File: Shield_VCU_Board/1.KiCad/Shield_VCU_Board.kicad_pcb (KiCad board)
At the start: 2 copper layers, 250.5 x 107.1 mm, 161 parts, among them J1 Conn_02x08_Odd_Even, J10 Main_Supply, J11 Conn_01x40_Socket, J13 Conn_Molex_TouchPanel, J14 CAN_OUT, J15 Conn_01x04_Socket, J2 Conn_02x10_Odd_Even, J3/1 NXP3, J4 Conn_02x08_Odd_Even, J5 Conn_02x10_Odd_Even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

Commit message: NewSupplyArchitecture - v0.1
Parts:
- removed C22, C23: 10uF, Capacitor_Tantalum_SMD:CP_EIA-2012-12_Kemet-R_HandSolder
- removed C46: 0.1uF, Capacitor_SMD:C_0805_2012Metric_Pad1.18x1.45mm_HandSolder
- removed D5, D6: 1N4002, Diode_SMD:D_SOD-123
- removed R57: 660, Resistor_SMD:R_1206_3216Metric_Pad1.30x1.75mm_HandSolder
- removed R58: 1.1k, Resistor_SMD:R_1206_3216Metric_Pad1.30x1.75mm_HandSolder
- removed U11: LM317_SOT-223, Package_TO_SOT_SMD:SOT-223-3_TabPin2
- added C45: 0.1uF, Capacitor_SMD:C_0805_2012Metric_Pad1.18x1.45mm_HandSolder, B.Cu at (44.6, 144.7)
- added C47: 10uF, Capacitor_SMD:C_1210_3225Metric_Pad1.33x2.70mm_HandSolder, B.Cu at (54.3, 147.6)
- added C48: 22uF, Capacitor_SMD:C_0805_2012Metric_Pad1.18x1.45mm_HandSolder, B.Cu at (54.1, 142.0)
- added C49: 0.1uF, Capacitor_SMD:C_0805_2012Metric_Pad1.18x1.45mm_HandSolder, B.Cu at (103.6, 134.5)
- added C50: 0.1uF, Capacitor_SMD:C_0805_2012Metric_Pad1.18x1.45mm_HandSolder, B.Cu at (99.4, 141.2)
- added C51: 22uF, Capacitor_SMD:C_0805_2012Metric_Pad1.18x1.45mm_HandSolder, B.Cu at (98.2, 132.9)
- added C52: 22uF, Capacitor_SMD:C_0805_2012Metric_Pad1.18x1.45mm_HandSolder, B.Cu at (52.1, 141.9)
- added C53: 22uF, Capacitor_SMD:C_0805_2012Metric_Pad1.18x1.45mm_HandSolder, B.Cu at (98.2, 130.8)
- added C54: 0.1uF, Capacitor_SMD:C_0805_2012Metric_Pad1.18x1.45mm_HandSolder, B.Cu at (51.5, 147.9)
- added C55: 10uF, Capacitor_SMD:C_1210_3225Metric_Pad1.33x2.70mm_HandSolder, B.Cu at (103.8, 131.3)
- added L3: 10uH, Inductor_SMD:L_Pulse_PA4340, B.Cu at (61.1, 143.8)
- added L4: 10uH, Inductor_SMD:L_Pulse_PA4340, B.Cu at (100.3, 126.0)
- added R59: 523k, Resistor_SMD:R_1206_3216Metric_Pad1.30x1.75mm_HandSolder, B.Cu at (39.0, 146.1)
- added R60: 100k, Resistor_SMD:R_1206_3216Metric_Pad1.30x1.75mm_HandSolder, B.Cu at (41.3, 146.1)
- added R65: 787k, Resistor_SMD:R_1206_3216Metric_Pad1.30x1.75mm_HandSolder, B.Cu at (101.6, 147.1)
- added R66: 100k, Resistor_SMD:R_1206_3216Metric_Pad1.30x1.75mm_HandSolder, B.Cu at (101.6, 144.5)
- added U12: TPS54202DDC, Package_TO_SOT_SMD:SOT-23-6, B.Cu at (46.7, 147.6)
- added U13: TPS54202DDC, Package_TO_SOT_SMD:SOT-23-6, B.Cu at (102.4, 139.4)
- moved J10 94.7 mm to (81.4, 145.8)
- moved V12 93.9 mm to (86.2, 143.3)
- moved D15 91.7 mm to (70.7, 144.6)
- moved D1 12.0 mm to (269.5, 63.4)
- moved D2 12.0 mm to (269.5, 76.5)
- moved D3 12.0 mm to (269.5, 89.6)
- moved D4 12.0 mm to (269.5, 102.8)
- moved Q1 11.1 mm to (262.9, 64.2)
- moved R1 11.1 mm to (259.8, 63.5)
- moved R18 10.2 mm to (264.1, 83.8)
- moved Q3 10.2 mm to (263.5, 86.9)
- moved R23 9.97 mm to (263.6, 98.6)
- moved Q4 9.97 mm to (262.9, 101.8)
- moved Q2 9.85 mm to (263.4, 74.2)
- moved R17 9.85 mm to (263.9, 71.1)
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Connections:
- net +12V renamed BAT+
- C27 pad 1: +7V -> +3.7V
- C29 pad 1: +7V -> +5.3V
- C31 pad 1: +7V -> +3.7V
- C33 pad 1: +7V -> +3.7V
- D10 pad 1: +7V -> +3.7V
- D7 pad 1: +7V -> +3.7V
- D8 pad 1: +7V -> +5.3V
- D9 pad 1: +7V -> +3.7V
- U5 pad 3: +7V -> +3.7V
- U6 pad 3: +7V -> +5.3V
- U8 pad 3: +7V -> +3.7V
- U9 pad 3: +7V -> +3.7V
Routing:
- net +7V: track 191.7 -> 0.00 mm
- net +3.7V: track 0.00 -> 187.7 mm
- net BAT+: track 324.1 -> 482.3 mm, vias 0 -> 2
- net +5.3V: track 0.00 -> 40.0 mm
- net LED1_PTD26: track 26.4 -> 48.6 mm
- net Net-(U13-SW): track 0.00 -> 22.0 mm, vias 0 -> 7
- net Net-(U12-SW): track 0.00 -> 21.8 mm, vias 0 -> 7
- net Net-(D5-A): track 13.7 -> 0.00 mm
- net GND: track 817.9 -> 829.7 mm, vias 51 -> 61
- net LED2_PTD29: track 35.4 -> 45.2 mm
- net LED3_PTD28: track 43.7 -> 53.1 mm
- net LED4_PTD31: track 53.7 -> 61.2 mm
- net Net-(U12-FB): track 0.00 -> 6.91 mm
- net Net-(U13-FB): track 0.00 -> 6.59 mm
- net Net-(U12-BOOT): track 0.00 -> 2.98 mm
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- added copper zone on B.Cu, net Net-(U12-SW)
- added copper zone on B.Cu, net Net-(U13-SW)
- removed copper zone on B.Cu, net +7V
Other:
- board text added: "BUTTON"
- board text added: "GND"
- board text added: "SPEAKER"
- board text added: "VCC"

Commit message: Shifting AUD 3V3 -> 5V0
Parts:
- R53: value 635R -> 1k
- U5: value TLV76133DCY -> TLV76150DCY
- moved V12 10.6 mm to (75.5, 143.3)
- moved U13 0.06 mm to (102.4, 139.5)
- renumbered AUDV3.3 to AUDV5
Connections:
- net 3V3_AUD renamed 5V_AUD
- net 3V3_SPKR renamed 5V0_SPKR
- C27 pad 1: +3.7V -> +5.3V
- D7 pad 1: +3.7V -> +5.3V
- U5 pad 3: +3.7V -> +5.3V
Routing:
- net +3.7V: track 187.7 -> 162.4 mm
- net +5.3V: track 40.0 -> 64.4 mm
- net AUD_SHDN: track 95.0 -> 97.2 mm
- net GND: track 829.7 -> 828.5 mm
- net LED_K: track 17.0 -> 17.5 mm
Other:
- outline, holes or cut-outs redrawn

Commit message: Major changes here
*GND planes;
*Supply paths
*Chip crystal removed
*Changes with INT/PD/SCK wiring
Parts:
- removed C14, C15: 27pF, Capacitor_SMD:C_0805_2012Metric_Pad1.18x1.45mm_HandSolder
- removed CS1, INT1, MISO1, MOSI1, PD1: TestPoint, TestPoint:TestPoint_Pad_D1.0mm
- removed Y2: SG-210STF, Oscillator:Oscillator_SMD_SeikoEpson_SG210-4Pin_2.5x2.0mm
- added J16: CAN_IN, Connector_JST:JST_XH_B2B-XH-A_1x02_P2.50mm_Vertical, B.Cu at (269.8, 131.8)
- moved C33 102.8 mm to (196.7, 77.8), turned to 90 degrees
- moved D10 92.9 mm to (190.1, 82.8), turned to 180 degrees
- moved U9 89.5 mm to (189.9, 77.8), turned to 180 degrees
- moved D11 77.8 mm to (184.9, 72.9), turned to 180 degrees
- moved C34 77.4 mm to (184.0, 76.0), turned to 90 degrees
- moved R22 71.9 mm to (181.4, 75.5), turned to 90 degrees
- moved DSPLV3.3 66.9 mm to (178.2, 77.3), turned to 0 degrees
- moved R20 61.9 mm to (116.8, 65.5)
- moved R16 53.1 mm to (122.8, 61.6)
- moved C35 52.8 mm to (120.5, 63.1), turned to -90 degrees
- moved SCK1 48.8 mm to (115.9, 53.9)
- moved U3 48.5 mm to (127.8, 59.1), turned to 0 degrees
- moved J10 47.2 mm to (35.2, 135.7), turned to -90 degrees
- moved R21 46.4 mm to (132.8, 65.9), turned to 0 degrees
- moved NT1 38.5 mm to (102.4, 47.9)
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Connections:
- R20 pad 2: FT_INT -> MC_INT
- R21 pad 2: FT_PD -> MC_PD
- U3 pad 1: MC_SPI_SCK -> MC_PD
- U3 pad 10: FT_INT -> unconnected-(U3-Y5-Pad10)
- U3 pad 11: MC_INT -> unconnected-(U3-A5-Pad11)
- U3 pad 2: FT_T_SCK -> FT_PD
- U3 pad 3: FT_MISO -> unconnected-(U3-A2-Pad3)
- U3 pad 4: MC_MISO -> unconnected-(U3-Y2-Pad4)
- U3 pad 8: MC_PD -> MC_SPI_SCK
- U3 pad 9: FT_PD -> FT_T_SCK
- U7 pad 13: FT_INT -> MC_INT
- U7 pad 16: Net-(U7-X1/CLK) -> unconnected-(U7-X1/CLK-Pad16)
- U7 pad 17: Net-(U7-X2) -> unconnected-(U7-X2-Pad17)
- U7 pad 6: FT_MISO -> MC_MISO
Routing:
- net (no net): track 0.00 -> 243.6 mm, vias 0 -> 20
- net GND: track 828.5 -> 602.6 mm, vias 61 -> 53
- net +3.7V: track 162.4 -> 275.3 mm, vias 0 -> 2
- net MC_MISO: track 5.28 -> 91.1 mm
- net FT_MISO: track 85.0 -> 0.00 mm
- net FT_INT: track 79.8 -> 0.00 mm
- net MC_INT: track 14.9 -> 90.3 mm
- net MC_PD: track 12.6 -> 74.6 mm
- net FT_PD: track 78.8 -> 17.5 mm
- net FT_MOSI: track 86.6 -> 29.4 mm
- net MC_MOSI: track 5.50 -> 60.2 mm
- net FT_CS: track 81.6 -> 31.0 mm
- net MC_CS: track 15.2 -> 62.0 mm
- net MC_SPI_SCK: track 5.53 -> 47.3 mm
- net FT_T_SCK: track 86.0 -> 46.1 mm
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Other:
- board text removed: "GND"
- board text removed: "VCC"

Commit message: AUDIO chip footprint corrected
Footprint uploaded from Mouser for exact reference.
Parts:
- added 3V7: 3V7, TestPoint:TestPoint_Pad_D1.0mm, B.Cu at (79.0, 126.8)
- added 5V3: 5V3, TestPoint:TestPoint_Pad_D1.0mm, B.Cu at (93.2, 135.6)
- added AUD+01: AUD+, TestPoint:TestPoint_Pad_D1.0mm, B.Cu at (87.8, 61.2)
- added AUD-01: AUD-, TestPoint:TestPoint_Pad_D1.0mm, B.Cu at (87.8, 58.2)
- added CS1: TestPoint, TestPoint:TestPoint_Pad_D1.0mm, B.Cu at (119.4, 58.3)
- added INT1: TestPoint, TestPoint:TestPoint_Pad_D1.0mm, B.Cu at (115.3, 67.7)
- added MISO1: TestPoint, TestPoint:TestPoint_Pad_D1.0mm, B.Cu at (111.0, 61.4)
- added MOSI1: TestPoint, TestPoint:TestPoint_Pad_D1.0mm, B.Cu at (115.1, 60.3)
- added PD1: TestPoint, TestPoint:TestPoint_Pad_D1.0mm, B.Cu at (118.2, 63.0)
- added R24: 220R, Resistor_SMD:R_1206_3216Metric_Pad1.30x1.75mm_HandSolder, B.Cu at (255.8, 64.9)
- added R25: 220R, Resistor_SMD:R_1206_3216Metric_Pad1.30x1.75mm_HandSolder, B.Cu at (258.6, 71.1)
- added R26: 220R, Resistor_SMD:R_1206_3216Metric_Pad1.30x1.75mm_HandSolder, B.Cu at (258.8, 83.8)
- added R28: 220R, Resistor_SMD:R_1206_3216Metric_Pad1.30x1.75mm_HandSolder, B.Cu at (259.4, 97.3)
- BAT+01: renamed from V12; value TestPoint -> BAT+
- J14, J16, J7, J8: footprint Connector_JST:JST_XH_B2B-XH-A_1x02_P2.50mm_Vertical -> Connector_JST:JST_PH_B2B-PH-K_1x02_P2.00mm_Vertical
- R3, R4, R5: value 220R -> 635R
- U4: footprint Package_SON:SON-8-1EP_3x2mm_P0.5mm_EP1.4x1.6mm -> TPA:TPS73601DRBR
- moved BAT+01 20.6 mm to (61.8, 143.6)
- moved C6 2.51 mm to (94.1, 56.7)
- moved C50 2.32 mm to (76.8, 144.4), turned to 90 degrees
- moved R15 2.25 mm to (91.6, 60.9)
- moved SCK1 1.35 mm to (114.5, 53.8)
- moved U4 1.22 mm to (95.5, 60.4)
- moved C4 1.01 mm to (100.8, 56.7)
- moved R12 1.01 mm to (99.3, 64.6)
- moved R13 0.96 mm to (93.7, 64.7)
- moved J8 0.90 mm to (81.4, 62.2)
- moved R66 0.55 mm to (74.4, 144.8)
- moved R10 0.47 mm to (102.8, 61.5)
- moved R11 0.47 mm to (102.8, 59.0)
- moved R65 0.30 mm to (72.0, 144.8)
- moved C5 0.24 mm to (99.3, 61.2)
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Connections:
- Q1 pad 1: LED1_PTD26 -> Net-(Q1-G)
- Q2 pad 1: LED2_PTD29 -> Net-(Q2-G)
- Q3 pad 1: LED3_PTD28 -> Net-(Q3-G)
- Q4 pad 1: LED4_PTD31 -> Net-(Q4-G)
- R1 pad 2: LED1_PTD26 -> Net-(Q1-G)
- R17 pad 2: LED2_PTD29 -> Net-(Q2-G)
- R18 pad 2: LED3_PTD28 -> Net-(Q3-G)
- R23 pad 2: LED4_PTD31 -> Net-(Q4-G)
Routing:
- net LED1_PTD26: track 48.6 -> 29.7 mm
- net FT_CS: track 31.0 -> 49.5 mm, vias 0 -> 1
- net GND: track 602.6 -> 586.9 mm, vias 53 -> 57
- net GNDA: track 54.8 -> 66.9 mm, vias 1 -> 5
- net LED3_PTD28: track 53.1 -> 45.6 mm
- net LED2_PTD29: track 45.2 -> 37.7 mm
- net LED4_PTD31: track 61.2 -> 55.3 mm
- net Net-(Q4-G): track 0.00 -> 4.87 mm
- net Net-(Q1-G): track 0.00 -> 4.71 mm
- net Net-(Q3-G): track 0.00 -> 4.43 mm
- net Net-(Q2-G): track 0.00 -> 4.40 mm
- net Net-(U4-IN-): track 15.3 -> 17.7 mm
- net +5.3V: track 78.3 -> 76.5 mm
- net Net-(U13-SW): track 22.0 -> 23.7 mm
- net Net-(U4-BYPASS): track 2.82 -> 4.12 mm
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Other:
- board text added: "Design: Gheorghe Stepuleac Revision: Viorel Stoica"
- board text removed: "Design: GHST Revision: VIST"

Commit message: GND planes correction
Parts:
- moved C12 1.04 mm to (129.9, 71.6)
- moved C13 1.04 mm to (129.9, 73.5)
- moved CS1 0.99 mm to (119.3, 59.3)
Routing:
- net GND: track 586.9 -> 846.5 mm, vias 57 -> 78
- net (no net): track 243.6 -> 0.00 mm, vias 20 -> 0
- net FT_CS: track 49.5 -> 30.7 mm, vias 1 -> 0
- net +1V2: track 9.52 -> 11.3 mm
- net Net-(RN8-R1.2): track 56.3 -> 57.4 mm
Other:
- outline, holes or cut-outs redrawn

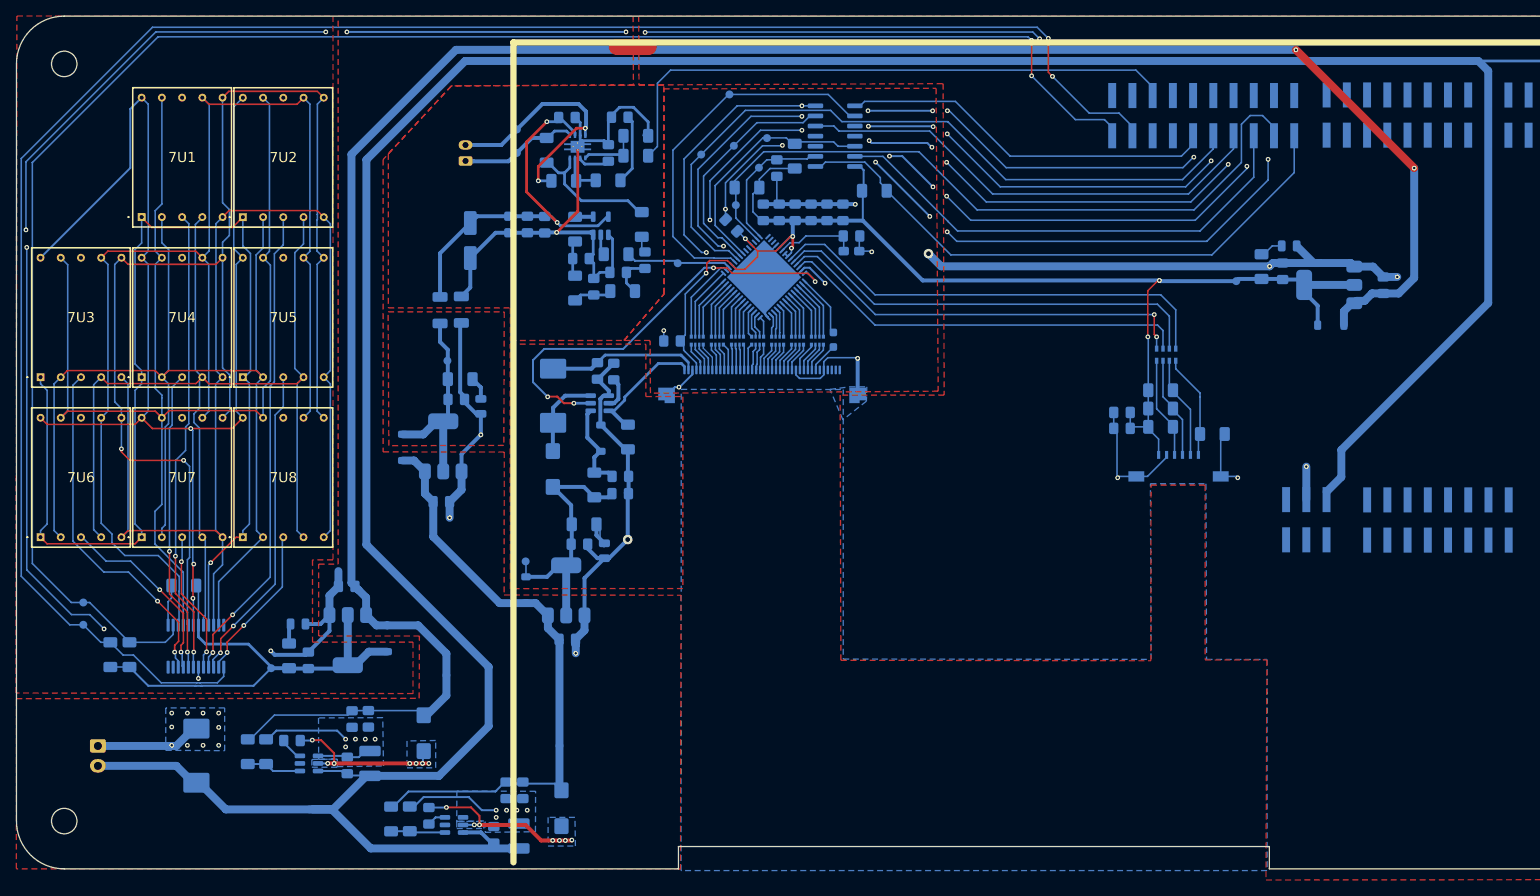
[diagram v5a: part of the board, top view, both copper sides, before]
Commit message: DNP 0 Ohm resistors added
DNP resistors added for the case where the Buck converters would have to be bridged.
The DNP resistors are rated by their size: 1206 - 3.0A -> 4.0A that should be more than enough for this Board
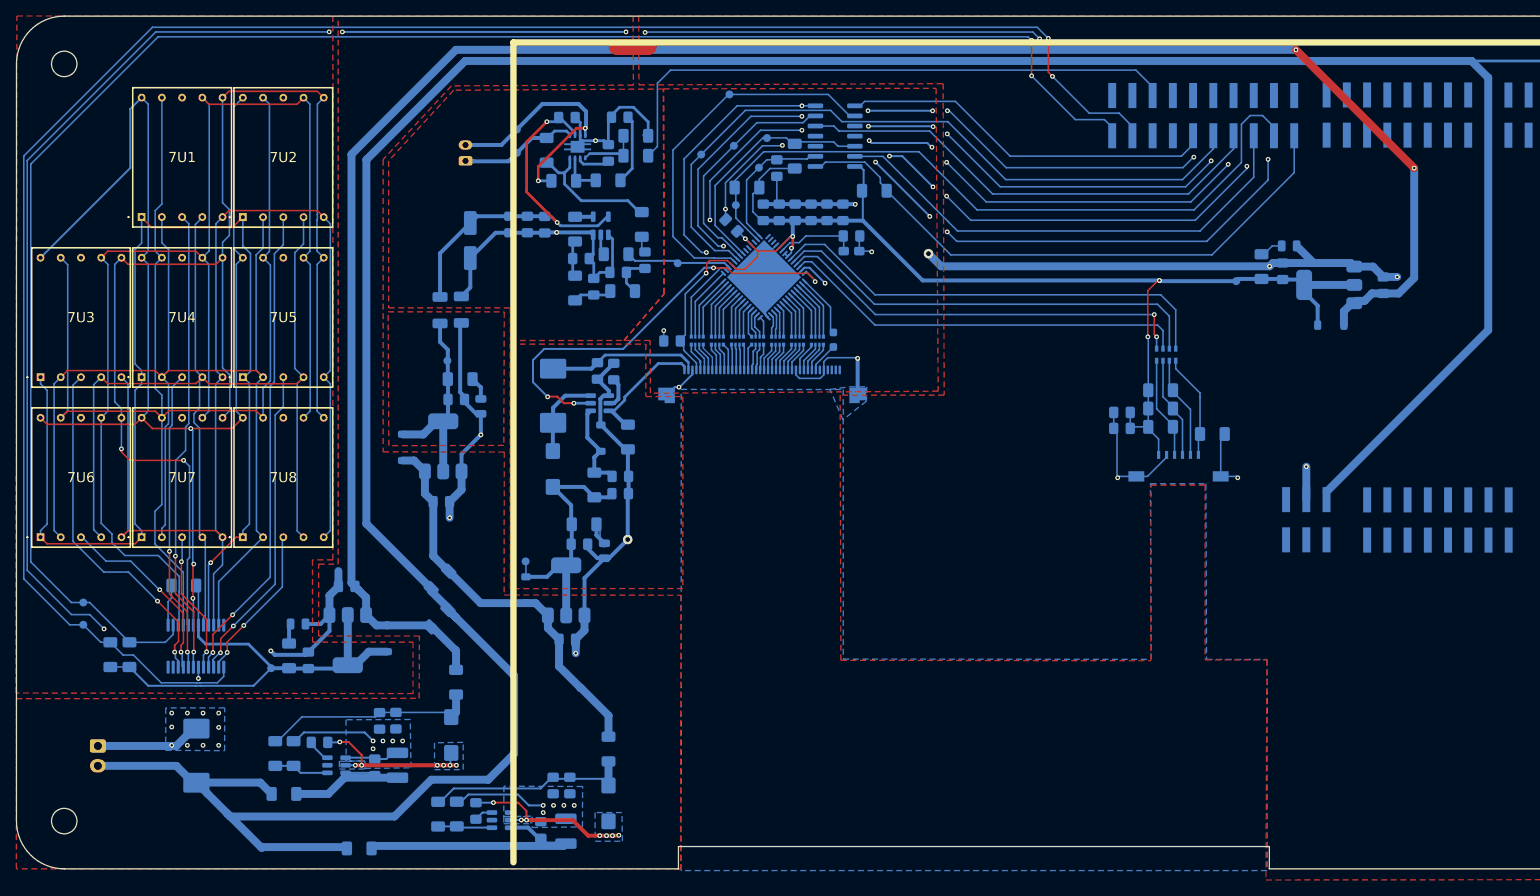
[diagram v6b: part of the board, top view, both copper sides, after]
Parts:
- added R29: 0R, Resistor_SMD:R_1206_3216Metric_Pad1.30x1.75mm_HandSolder, B.Cu at (78.2, 114.8)
- added R30: 0R, Resistor_SMD:R_1206_3216Metric_Pad1.30x1.75mm_HandSolder, B.Cu at (78.1, 119.6)
- added R31: 0R, Resistor_SMD:R_1206_3216Metric_Pad1.30x1.75mm_HandSolder, B.Cu at (58.6, 141.7)
- added R32: 0R, Resistor_SMD:R_1206_3216Metric_Pad1.30x1.75mm_HandSolder, B.Cu at (68.0, 148.5)
- added R33: 0R, Resistor_SMD:R_1206_3216Metric_Pad1.30x1.75mm_HandSolder, B.Cu at (80.2, 127.7)
- added R34: 0R, Resistor_SMD:R_1206_3216Metric_Pad1.30x1.75mm_HandSolder, B.Cu at (99.4, 136.1)
- moved 5V3 7.74 mm to (95.8, 128.4)
- moved BAT+01 7.71 mm to (55.8, 148.5)
- moved C50 5.94 mm to (82.7, 143.8)
- moved C51 5.94 mm to (92.4, 140.6)
- moved C53 5.94 mm to (94.5, 140.6)
- moved L4 5.94 mm to (99.4, 142.9)
- moved R65 5.94 mm to (78.0, 144.2)
- moved C49 5.94 mm to (90.9, 146.2)
- moved U13 5.94 mm to (85.9, 145.0)
- moved C55 5.94 mm to (94.0, 146.4)
- moved R66 5.94 mm to (80.3, 144.2)
- moved C47 3.46 mm to (72.9, 138.1)
- moved C48 3.46 mm to (72.7, 132.5)
- moved R59 3.46 mm to (57.5, 136.6)
- moved R60 3.46 mm to (59.8, 136.6)
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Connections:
- C47 pad 1: BAT+ -> Net-(U12-VIN)
- C48 pad 1: +3.7V -> Net-(C48-Pad1)
- C49 pad 1: BAT+ -> Net-(U13-VIN)
- C51 pad 1: +5.3V -> Net-(C51-Pad1)
- C52 pad 1: +3.7V -> Net-(C48-Pad1)
- C53 pad 1: +5.3V -> Net-(C51-Pad1)
- C54 pad 1: BAT+ -> Net-(U12-VIN)
- C55 pad 1: BAT+ -> Net-(U13-VIN)
- L3 pad 2: +3.7V -> Net-(C48-Pad1)
- L4 pad 2: +5.3V -> Net-(C51-Pad1)
- R59 pad 2: +3.7V -> Net-(C48-Pad1)
- R65 pad 2: +5.3V -> Net-(C51-Pad1)
- U12 pad 3: BAT+ -> Net-(U12-VIN)
- U13 pad 3: BAT+ -> Net-(U13-VIN)
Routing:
- net Net-(U13-VIN): track 0.00 -> 32.7 mm
- net +3.7V: track 275.2 -> 245.7 mm
- net Net-(C48-Pad1): track 0.00 -> 27.3 mm
- net Net-(C51-Pad1): track 0.00 -> 25.8 mm
- net +5.3V: track 76.5 -> 51.1 mm
- net Net-(U12-VIN): track 0.00 -> 20.9 mm
- net GNDA: track 66.9 -> 55.5 mm, vias 5 -> 2
- net BAT+: track 489.9 -> 482.6 mm
- net GND: track 846.5 -> 849.4 mm, vias 78 -> 76

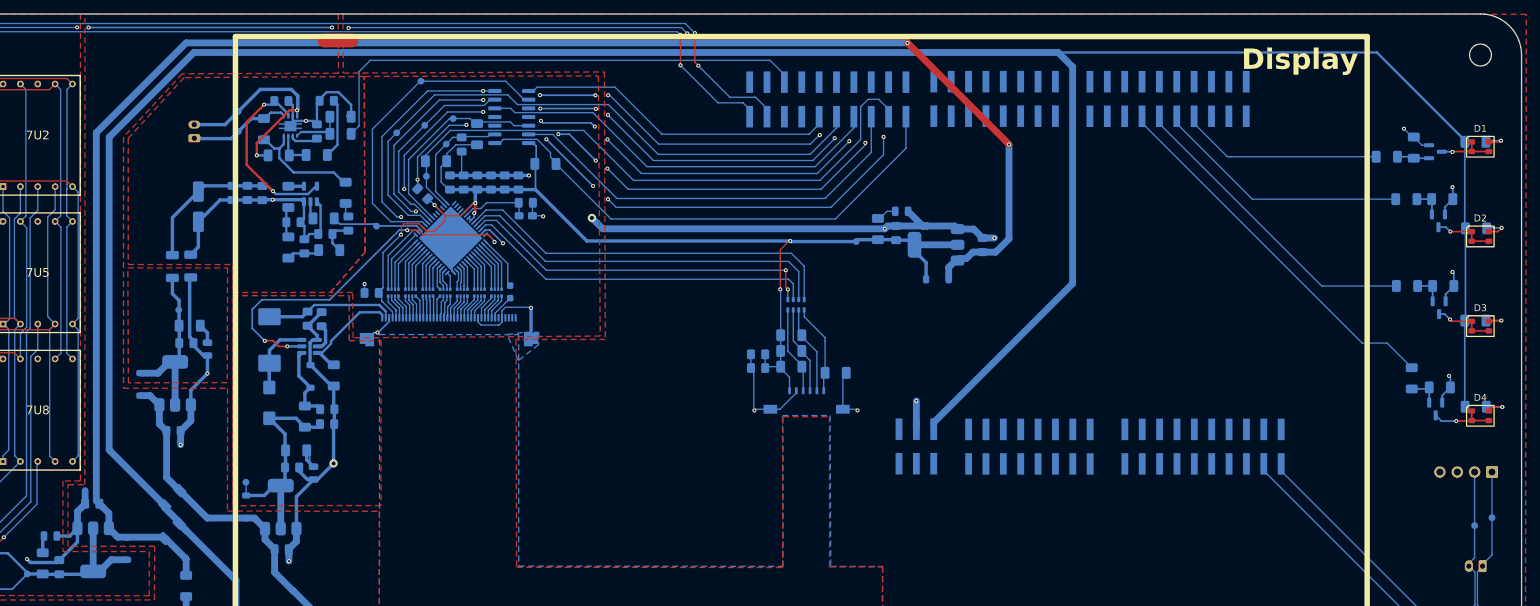
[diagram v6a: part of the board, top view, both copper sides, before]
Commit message: MainGND plane corrections
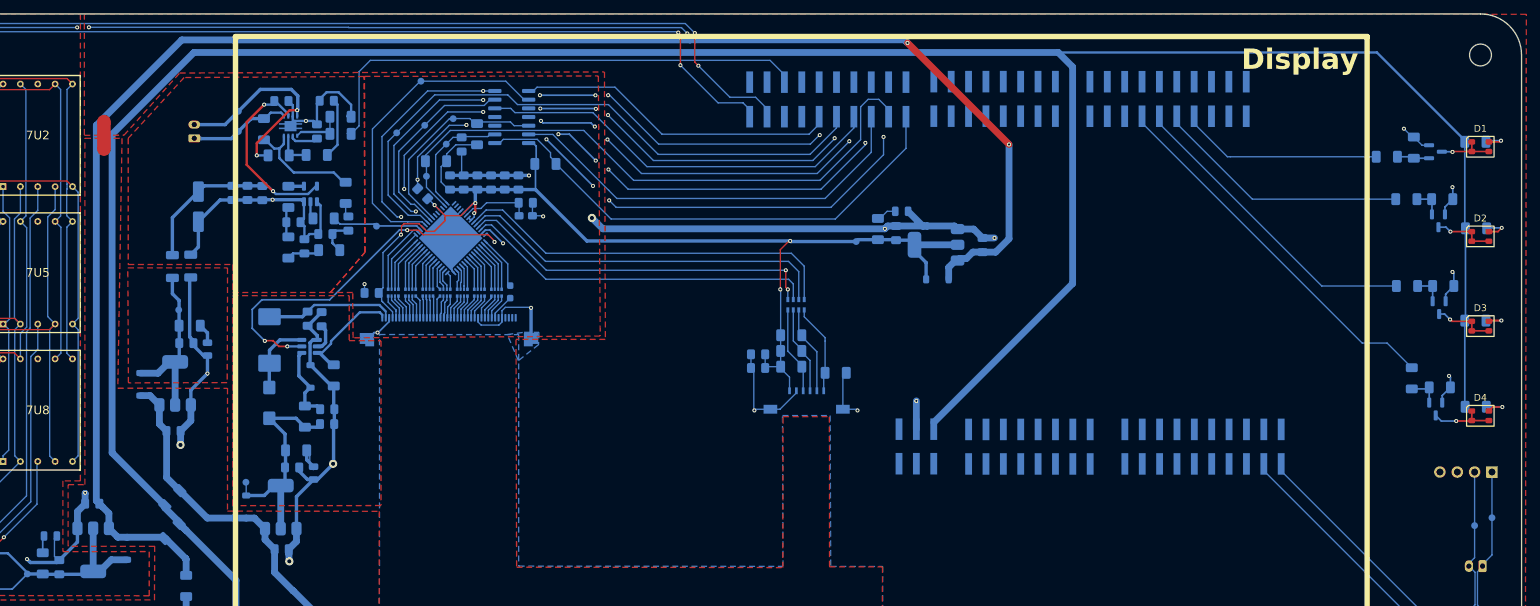
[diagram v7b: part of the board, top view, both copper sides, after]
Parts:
- moved NT1 36.9 mm to (68.2, 61.8), turned to 90 degrees
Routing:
- net GND: track 849.4 -> 851.5 mm, vias 76 -> 75
- net +3.7V: track 245.7 -> 246.7 mm
